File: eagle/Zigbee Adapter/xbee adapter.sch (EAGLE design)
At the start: 11 parts, among them J3 POW_CONNECTMALE

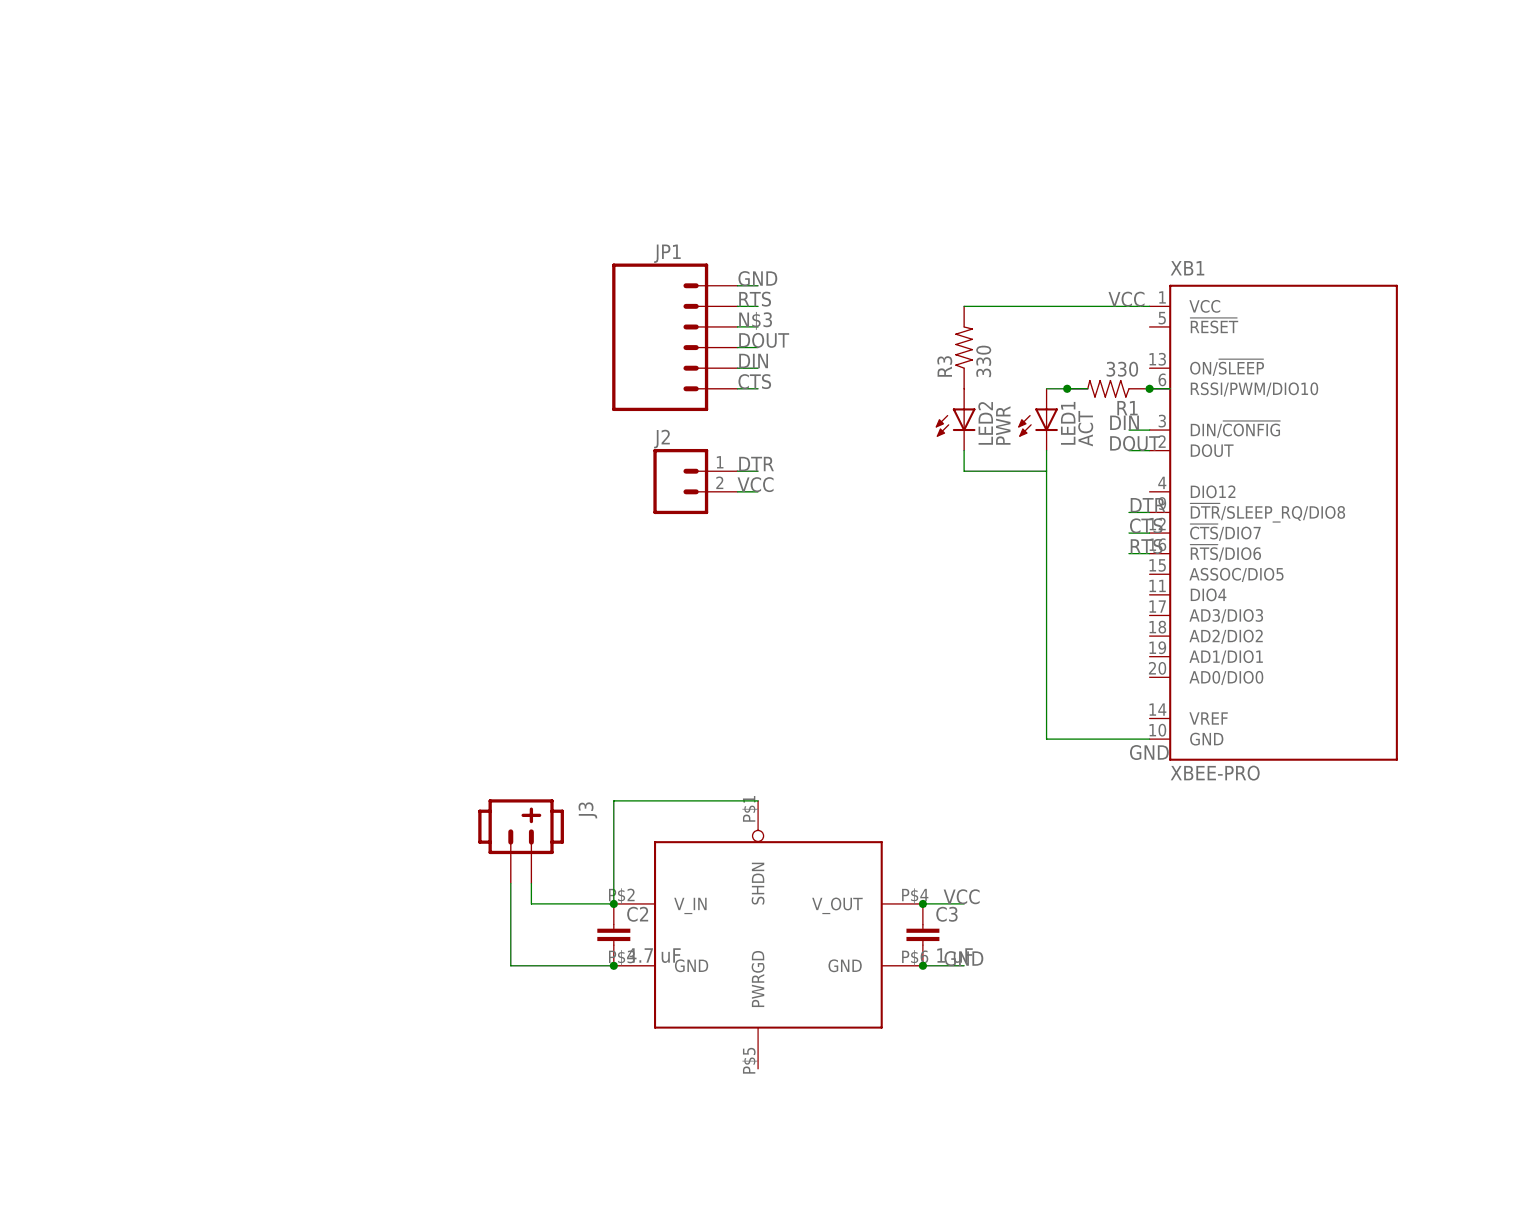
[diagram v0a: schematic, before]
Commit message: New rs232 adapter for xbee.
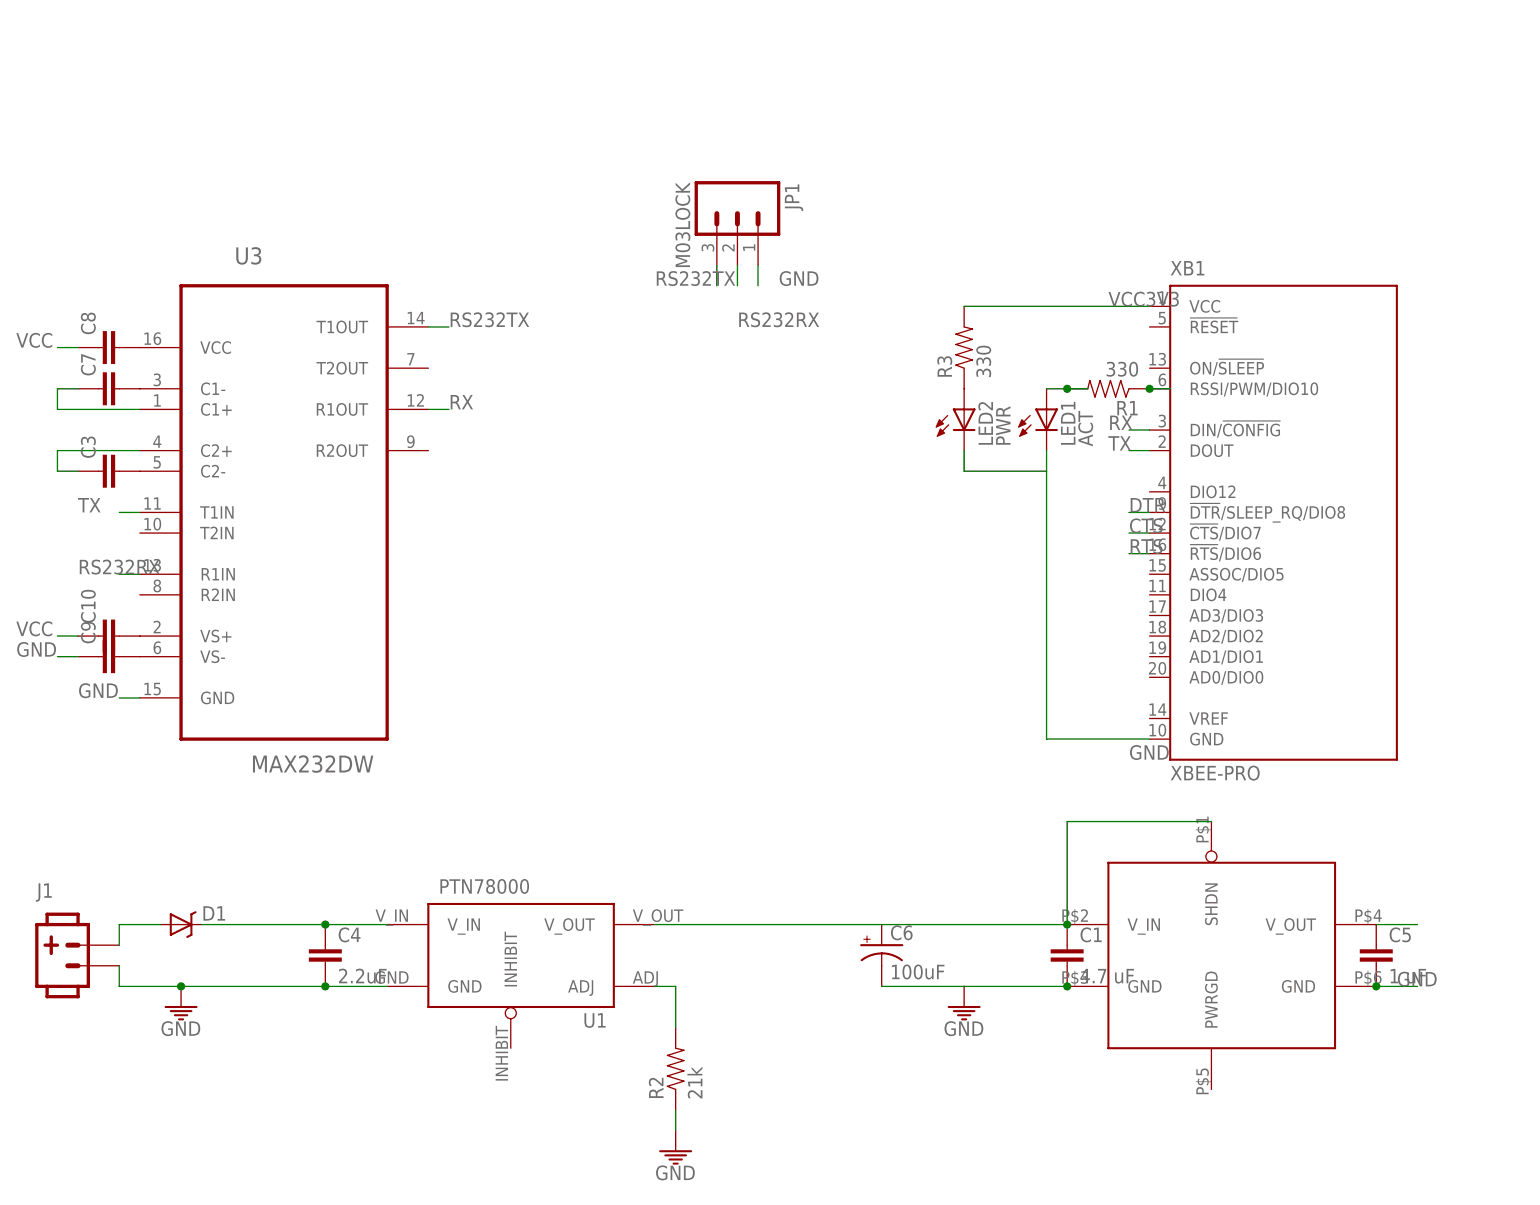
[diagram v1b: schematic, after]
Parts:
- removed C2: 4.7 uF, ASL:CAP1206
- removed J2: (no value), ASL:M02LOCK
- removed J3: POW_CONNECTMALE, ASL:POW_CONNECTMALE
- removed U$1: MCP1826, ASL:MCP1826
- added C1: 4.7 uF, ASL:CAP1206
- added C10, C7, C8, C9: (no value), ASL:CAP1206
- added C4: 2.2uF, CMPE118lib:CAP1206
- added C5: 1 uF, ASL:CAP1206
- added C6: 100uF, CMPE118lib:CAP_POL
- added D1: DIODE-SCHOTTKY240A, CMPE118lib:DIODE-SCHOTTKY240A
- added J1: POW_CONNECTMALE, CMPE118lib:POW_CONNECTMALE
- added R2: 21k, CMPE118lib:RESISTOR0805-RES
- added U$2: MCP1826, ASL:MCP1826
- added U1: PTN78000, ASL:PTN78000THROUGH-HOLE
- added U3: MAX232DW, Texas Instruments_By_element14_Batch_1:MAX232DW
- C3: value 1 uF -> (none)
- JP1: value (none) -> M03LOCK; device ASL:M06SIP -> ASL:M03LOCK
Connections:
- removed net DIN: JP1.5, XB1.DIN/!CONFIG
- removed net DOUT: JP1.4, XB1.DOUT
- removed net N$3: JP1.3
- new net N$1: C3.2, U3.C2-
- new net N$10: C8.2, U3.VCC
- new net N$11: C9.2, U3.VS-
- new net N$12: C10.2, U3.VS+
- new net N$15: C3.1, U3.C2+
- new net N$16: C7.1, U3.C1+
- new net N$6: R2.2, U1.ADJ
- new net N$7: C7.2, U3.C1-
- new net N$8: C4.1, D1.C, U1.V_IN
- new net N$9: D1.A, J1.1
- new net RS232RX: JP1.2, U3.R1IN
- new net RS232TX: JP1.3, U3.T1OUT
- new net RX: U3.R1OUT, XB1.DIN/!CONFIG
- new net TX: U3.T1IN, XB1.DOUT
- new net VCC3V3: C5.1, R3.2, U$2.V_OUT, XB1.VCC
- net CTS: no longer JP1.6
- net DTR: no longer J2.2
- net GND: now also C1.2, C4.2, C5.2, C6.-, C9.1, J1.2, R2.1, U$2.GND@3, U$2.GND@6, U1.GND, U3.GND; no longer C2.2, C3.2, J3.2, U$1.GND@3, U$1.GND@6
- net RTS: no longer JP1.2
- net VCC: now also C1.1, C10.1, C6.+, C8.1, U$2.SHDN, U$2.V_IN, U1.V_OUT; no longer C2.1, C3.1, J2.1, J3.1, R3.2, U$1.SHDN, U$1.V_IN, U$1.V_OUT, XB1.VCC
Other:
- moved on the sheet: C3

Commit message: New 1-Axis Test BLDC breakout for gluon stab
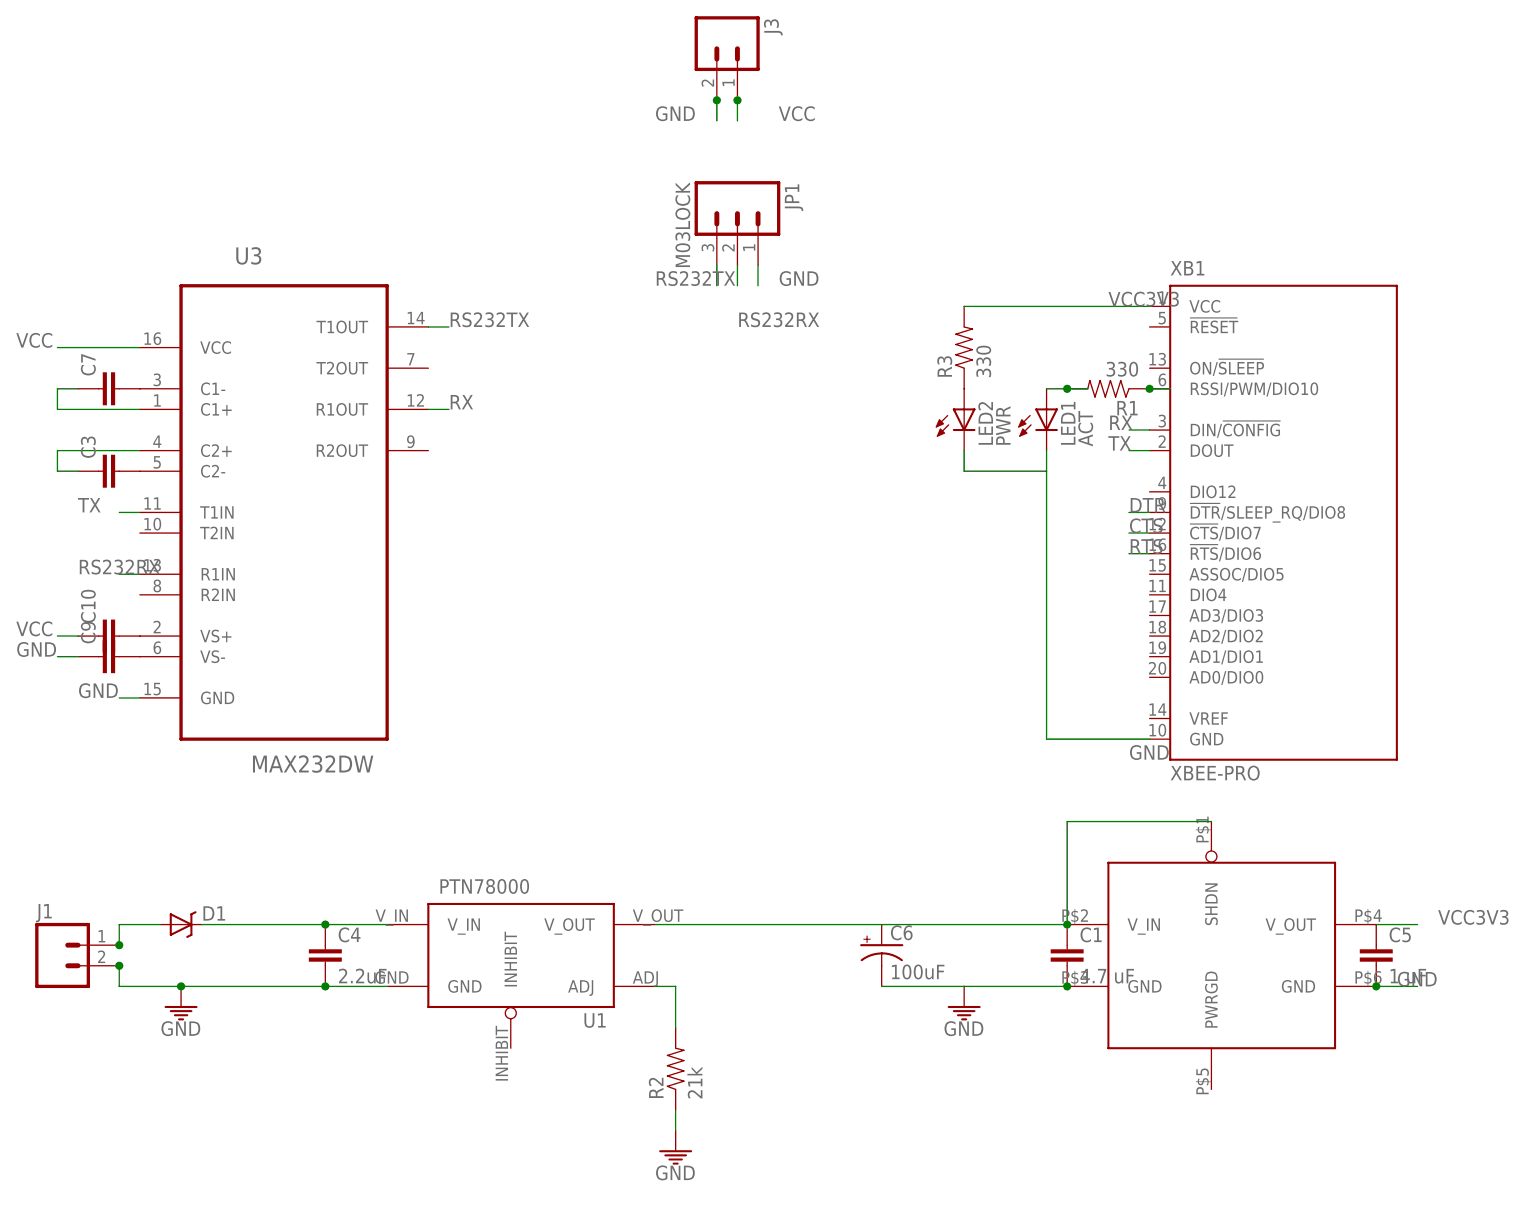
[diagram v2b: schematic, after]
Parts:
- removed C8: (no value), ASL:CAP1206
- added J3: (no value), ASL:M023.5MM-NO_SILK
- J1: value POW_CONNECTMALE -> (none); device CMPE118lib:POW_CONNECTMALE -> ASL:M023.5MM-NO_SILK
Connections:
- removed net N$10: C8.2, U3.VCC
- net GND: now also J1.1, J3.1; no longer J1.2
- net N$9: now also J1.2; no longer J1.1
- net VCC: now also J3.2, U3.VCC; no longer C8.1
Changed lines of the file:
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@@
 <part name="R1" library="ASL" deviceset="RESISTOR" device="0805-RES" value="330"/>
 <part name="U1" library="ASL" deviceset="PTN78000" device="THROUGH-HOLE" value="PTN78000"/>
-<part name="J1" library="CMPE118lib" deviceset="POW_CONNECT" device="MALE"/>
 <part name="D1" library="CMPE118lib" deviceset="DIODE-SCHOTTKY" device="240A"/>
 <part name="C4" library="CMPE118lib" deviceset="CAP" device="1206" value="2.2uF"/>
@@
 <part name="C3" library="ASL" deviceset="CAP" device="1206"/>
 <part name="C7" library="ASL" deviceset="CAP" device="1206"/>
-<part name="C8" library="ASL" deviceset="CAP" device="1206"/>
 <part name="C9" library="ASL" deviceset="CAP" device="1206"/>
 <part name="C10" library="ASL" deviceset="CAP" device="1206"/>
 <part name="JP1" library="ASL" deviceset="M03" device="LOCK"/>
+<part name="J1" library="ASL" deviceset="M02" device="3.5MM-NO_SILK"/>
+<part name="J3" library="ASL" deviceset="M02" device="3.5MM-NO_SILK"/>
 </parts>
 <sheets>
@@
 <instance part="R1" gate="G$1" x="55.88" y="99.06" rot="R180"/>
 <instance part="U1" gate="G$1" x="-20.32" y="27.94"/>
-<instance part="J1" gate="G$1" x="-76.2" y="25.4"/>
 <instance part="D1" gate="G$1" x="-58.42" y="33.02" smashed="yes">
 <attribute name="NAME" x="-55.88" y="33.5026" size="1.778" layer="95"/>
@@
 <instance part="C3" gate="G$1" x="-66.04" y="88.9" rot="R90"/>
 <instance part="C7" gate="G$1" x="-66.04" y="99.06" rot="R90"/>
-<instance part="C8" gate="G$1" x="-66.04" y="104.14" rot="R90"/>
 <instance part="C9" gate="G$1" x="-66.04" y="66.04" rot="R90"/>
 <instance part="C10" gate="G$1" x="-66.04" y="68.58" rot="R90"/>
 <instance part="JP1" gate="G$1" x="10.16" y="121.92" rot="R270"/>
+<instance part="J1" gate="G$1" x="-76.2" y="25.4"/>
+<instance part="J3" gate="G$1" x="5.08" y="144.78" rot="R270"/>
 </instances>
 <busses>
@@
 </segment>
 <segment>
-<pinref part="C8" gate="G$1" pin="1"/>
-<wire x1="-71.12" y1="104.14" x2="-73.66" y2="104.14" width="0.2032" layer="91"/>
 <label x="-78.74" y="104.14" size="1.778" layer="95"/>
+<pinref part="U3" gate="A" pin="VCC"/>
+<wire x1="-73.66" y1="104.14" x2="-63.5" y2="104.14" width="0.2032" layer="91"/>
+</segment>
+<segment>
+<wire x1="10.16" y1="134.62" x2="10.16" y2="132.08" width="0.2032" layer="91"/>
+<label x="15.24" y="132.08" size="1.778" layer="95"/>
+<pinref part="J3" gate="G$1" pin="2"/>
+<junction x="10.16" y="134.62"/>
 </segment>
 </net>
@@
 <pinref part="C4" gate="G$1" pin="2"/>
 <pinref part="GND2" gate="1" pin="GND"/>
-<pinref part="J1" gate="G$1" pin="2"/>
+<pinref part="J1" gate="G$1" pin="1"/>
+<junction x="-66.04" y="27.94"/>
 </segment>
 <segment>
@@
 <wire x1="12.7" y1="114.3" x2="12.7" y2="111.76" width="0.2032" layer="91"/>
 <label x="15.24" y="111.76" size="1.778" layer="95"/>
+</segment>
+<segment>
+<wire x1="7.62" y1="134.62" x2="7.62" y2="132.08" width="0.2032" layer="91"/>
+<label x="0" y="132.08" size="1.778" layer="95"/>
+<pinref part="J3" gate="G$1" pin="1"/>
+<junction x="7.62" y="134.62"/>
 </segment>
 </net>
@@
 <wire x1="-66.04" y1="30.48" x2="-66.04" y2="33.02" width="0.1524" layer="91"/>
 <wire x1="-60.96" y1="33.02" x2="-66.04" y2="33.02" width="0.1524" layer="91"/>
-<pinref part="J1" gate="G$1" pin="1"/>
 <pinref part="D1" gate="G$1" pin="A"/>
+<pinref part="J1" gate="G$1" pin="2"/>
+<junction x="-66.04" y="30.48"/>
 </segment>
 </net>
@@
 <pinref part="C5" gate="G$1" pin="1"/>
 <wire x1="88.9" y1="33.02" x2="93.98" y2="33.02" width="0.2032" layer="91"/>
+<label x="96.52" y="33.02" size="1.778" layer="95"/>
 </segment>
 <segment>
@@
 </segment>
 </net>
-<net name="N$10" class="0">
-<segment>
-<pinref part="U3" gate="A" pin="VCC"/>
-<pinref part="C8" gate="G$1" pin="2"/>
-</segment>
-</net>
